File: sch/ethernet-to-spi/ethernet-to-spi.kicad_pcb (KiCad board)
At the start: 2 copper layers, 113 x 32 mm, 34 parts, among them J1 G8X-188S7-BP, J2 mosi, J3 sck_tx, J4 mosi_tx, J5 cs, J6 sck, J7 vcc, J8 gnd, Q1 2N7002, Q2 2N7002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

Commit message: Add level shifters for inputs
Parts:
- added Q3: 2N7002, Package_TO_SOT_SMD:SOT-23, F.Cu at (110.0, 123.6)
- added Q4: 2N7002, Package_TO_SOT_SMD:SOT-23, F.Cu at (109.3, 129.4)
- added R6: 1k, Resistor_SMD:R_0805_2012Metric, F.Cu at (107.3, 119.9)
- added R7: 1k, Resistor_SMD:R_0805_2012Metric, F.Cu at (105.7, 127.8)
- moved C3 7.47 mm to (98.5, 109.9)
- moved C2 6.28 mm to (98.0, 114.1)
- moved C4 4.35 mm to (94.9, 106.7)
- moved U3 4.35 mm to (101.9, 109.9)
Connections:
- U1 pad 1: Net-(J3-Pad1) -> Net-(U1-Pad1)
- U1 pad 2: Net-(J4-Pad1) -> Net-(U1-Pad2)
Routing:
- net VCC: track 179.3 -> 198.9 mm
- net Net-(U1-Pad2): track 0.00 -> 16.6 mm
- net Net-(C3-Pad2): track 14.5 -> 2.50 mm
- net Net-(C2-Pad2): track 14.6 -> 3.59 mm
- net Net-(U1-Pad1): track 0.00 -> 9.73 mm
- net Net-(C3-Pad1): track 10.00 -> 17.7 mm
- net Net-(C2-Pad1): track 7.58 -> 14.3 mm
- net Net-(J4-Pad1): track 9.43 -> 3.38 mm
- net Net-(U1-Pad3): track 36.6 -> 41.0 mm
- net /line: track 50.8 -> 55.2 mm
- net Net-(J1-Pad2): track 21.5 -> 19.2 mm
- net Net-(R2-Pad2): track 13.0 -> 11.3 mm
- net Net-(J3-Pad1): track 4.70 -> 3.06 mm

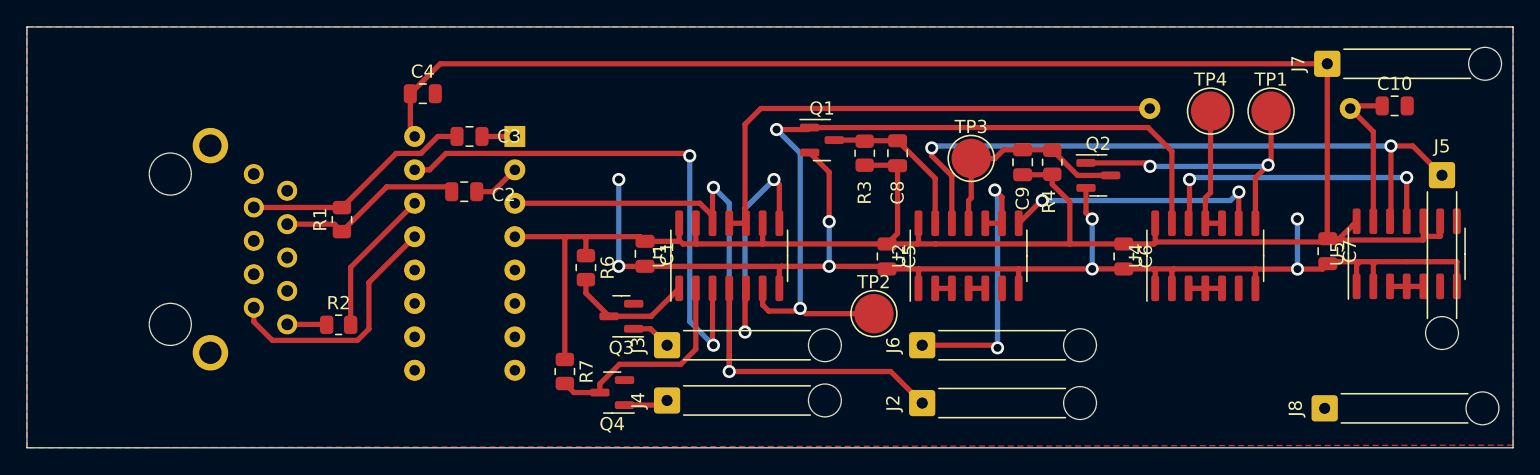
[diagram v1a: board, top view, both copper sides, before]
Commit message: Update capacitor value for 75 nS delay
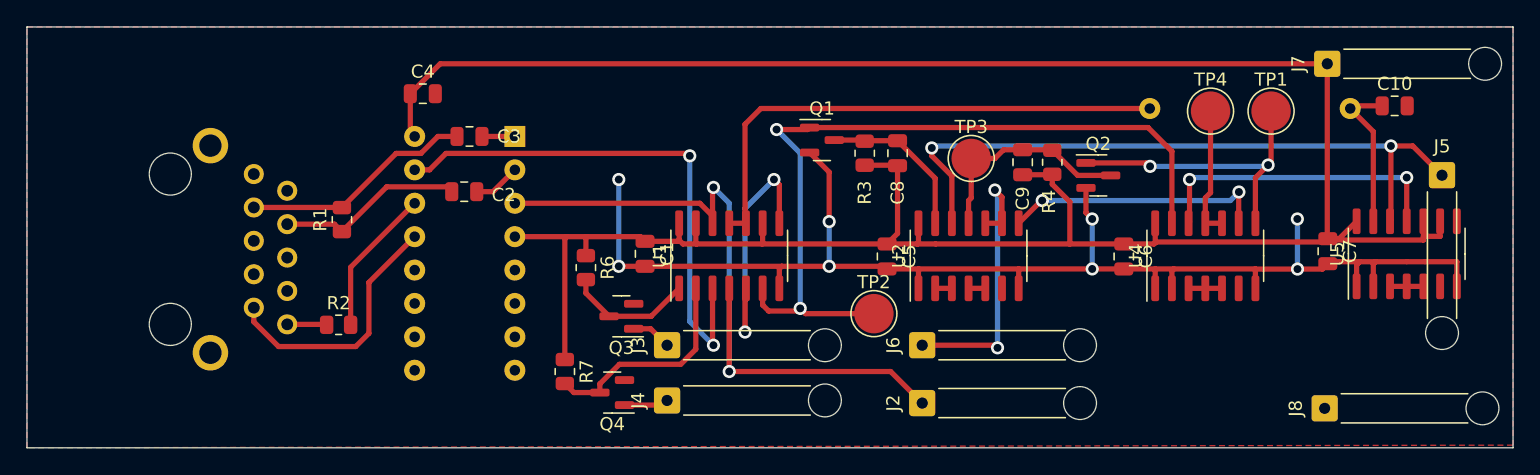
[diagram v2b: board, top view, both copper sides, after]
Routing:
- net Net-(J1-Pad2): track 19.2 -> 19.8 mm
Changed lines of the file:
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@@
     (aux_axis_origin 64.8 133.6)
     (pcbplotparams
-      (layerselection 0x00010fc_ffffffff)
+      (layerselection 0x0001000_7fffffff)
       (disableapertmacros false)
       (usegerberextensions false)
       (usegerberattributes true)
       (usegerberadvancedattributes true)
-      (creategerberjobfile true)
+      (creategerberjobfile false)
       (svguseinch false)
       (svgprecision 6)
@@
       (viasonmask false)
       (mode 1)
-      (useauxorigin false)
+      (useauxorigin true)
       (hpglpennumber 1)
       (hpglpenspeed 20)
@@
       (outputformat 1)
       (mirror false)
-      (drillshape 1)
+      (drillshape 0)
       (scaleselection 1)
-      (outputdirectory "")
+      (outputdirectory "gerber/")
     )
   )
@@
     (fp_line (start 1 -0.625) (end 1 0.625) (layer "F.Fab") (width 0.1))
     (fp_line (start -1 -0.625) (end 1 -0.625) (layer "F.Fab") (width 0.1))
-    (pad "1" smd roundrect (at -0.9125 0 270) (size 1.025 1.4) (layers "F.Cu" "F.Paste" "F.Mask") (roundrect_rratio 0.243902)
+    (pad "1" smd roundrect (at -0.9125 0 270) (size 1.025 1.4) (layers "F.Cu" "F.Paste" "F.Mask") (roundrect_rratio 0.243902439)
       (net 1 "VCC") (pintype "passive"))
-    (pad "2" smd roundrect (at 0.9125 0 270) (size 1.025 1.4) (layers "F.Cu" "F.Paste" "F.Mask") (roundrect_rratio 0.243902)
+    (pad "2" smd roundrect (at 0.9125 0 270) (size 1.025 1.4) (layers "F.Cu" "F.Paste" "F.Mask") (roundrect_rratio 0.243902439)
       (net 42 "Net-(U1-Pad2)") (pintype "passive"))
     (model "${KICAD6_3DMODEL_DIR}/Resistor_SMD.3dshapes/R_0805_2012Metric.wrl"
@@
     (fp_line (start 1 -0.625) (end 1 0.625) (layer "F.Fab") (width 0.1))
     (fp_line (start -1 -0.625) (end 1 -0.625) (layer "F.Fab") (width 0.1))
-    (pad "1" smd roundrect (at -0.9125 0 90) (size 1.025 1.4) (layers "F.Cu" "F.Paste" "F.Mask") (roundrect_rratio 0.243902)
+    (pad "1" smd roundrect (at -0.9125 0 90) (size 1.025 1.4) (layers "F.Cu" "F.Paste" "F.Mask") (roundrect_rratio 0.243902439)
       (net 1 "VCC") (pintype "passive"))
-    (pad "2" smd roundrect (at 0.9125 0 90) (size 1.025 1.4) (layers "F.Cu" "F.Paste" "F.Mask") (roundrect_rratio 0.243902)
+    (pad "2" smd roundrect (at 0.9125 0 90) (size 1.025 1.4) (layers "F.Cu" "F.Paste" "F.Mask") (roundrect_rratio 0.243902439)
       (net 7 "Net-(C8-Pad2)") (pintype "passive"))
     (model "${KICAD6_3DMODEL_DIR}/Resistor_SMD.3dshapes/R_0805_2012Metric.wrl"
@@
     (fp_line (start -1 0.625) (end -1 -0.625) (layer "F.Fab") (width 0.1))
     (fp_line (start 1 0.625) (end -1 0.625) (layer "F.Fab") (width 0.1))
-    (pad "1" smd roundrect (at -0.9125 0 90) (size 1.025 1.4) (layers "F.Cu" "F.Paste" "F.Mask") (roundrect_rratio 0.243902)
+    (pad "1" smd roundrect (at -0.9125 0 90) (size 1.025 1.4) (layers "F.Cu" "F.Paste" "F.Mask") (roundrect_rratio 0.243902439)
       (net 3 "Net-(C2-Pad1)") (pintype "passive"))
-    (pad "2" smd roundrect (at 0.9125 0 90) (size 1.025 1.4) (layers "F.Cu" "F.Paste" "F.Mask") (roundrect_rratio 0.243902)
+    (pad "2" smd roundrect (at 0.9125 0 90) (size 1.025 1.4) (layers "F.Cu" "F.Paste" "F.Mask") (roundrect_rratio 0.243902439)
       (net 5 "Net-(C3-Pad1)") (pintype "passive"))
     (model "${KICAD6_3DMODEL_DIR}/Resistor_SMD.3dshapes/R_0805_2012Metric.wrl"
@@
     (fp_line (start -1 0.625) (end -1 -0.625) (layer "F.Fab") (width 0.1))
     (fp_line (start -1 -0.625) (end 1 -0.625) (layer "F.Fab") (width 0.1))
-    (pad "1" smd roundrect (at -0.9125 0) (size 1.025 1.4) (layers "F.Cu" "F.Paste" "F.Mask") (roundrect_rratio 0.243902)
+    (pad "1" smd roundrect (at -0.9125 0) (size 1.025 1.4) (layers "F.Cu" "F.Paste" "F.Mask") (roundrect_rratio 0.243902439)
       (net 9 "Net-(J1-Pad1)") (pintype "passive"))
-    (pad "2" smd roundrect (at 0.9125 0) (size 1.025 1.4) (layers "F.Cu" "F.Paste" "F.Mask") (roundrect_rratio 0.243902)
+    (pad "2" smd roundrect (at 0.9125 0) (size 1.025 1.4) (layers "F.Cu" "F.Paste" "F.Mask") (roundrect_rratio 0.243902439)
       (net 21 "Net-(R2-Pad2)") (pintype "passive"))
     (model "${KICAD6_3DMODEL_DIR}/Resistor_SMD.3dshapes/R_0805_2012Metric.wrl"
@@
     (fp_line (start 1 -0.625) (end 1 0.625) (layer "F.Fab") (width 0.1))
     (fp_line (start -1 0.625) (end -1 -0.625) (layer "F.Fab") (width 0.1))
-    (pad "1" smd roundrect (at -0.9125 0 90) (size 1.025 1.4) (layers "F.Cu" "F.Paste" "F.Mask") (roundrect_rratio 0.243902)
+    (pad "1" smd roundrect (at -0.9125 0 90) (size 1.025 1.4) (layers "F.Cu" "F.Paste" "F.Mask") (roundrect_rratio 0.243902439)
       (net 1 "VCC") (pintype "passive"))
-    (pad "2" smd roundrect (at 0.9125 0 90) (size 1.025 1.4) (layers "F.Cu" "F.Paste" "F.Mask") (roundrect_rratio 0.243902)
+    (pad "2" smd roundrect (at 0.9125 0 90) (size 1.025 1.4) (layers "F.Cu" "F.Paste" "F.Mask") (roundrect_rratio 0.243902439)
       (net 8 "Net-(C9-Pad2)") (pintype "passive"))
     (model "${KICAD6_3DMODEL_DIR}/Resistor_SMD.3dshapes/R_0805_2012Metric.wrl"
@@
     (fp_line (start 1 0.625) (end -1 0.625) (layer "F.Fab") (width 0.1))
     (fp_line (start -1 -0.625) (end 1 -0.625) (layer "F.Fab") (width 0.1))
-    (pad "1" smd roundrect (at -0.9125 0 270) (size 1.025 1.4) (layers "F.Cu" "F.Paste" "F.Mask") (roundrect_rratio 0.243902)
+    (pad "1" smd roundrect (at -0.9125 0 270) (size 1.025 1.4) (layers "F.Cu" "F.Paste" "F.Mask") (roundrect_rratio 0.243902439)
       (net 1 "VCC") (pintype "passive"))
-    (pad "2" smd roundrect (at 0.9125 0 270) (size 1.025 1.4) (layers "F.Cu" "F.Paste" "F.Mask") (roundrect_rratio 0.243902)
+    (pad "2" smd roundrect (at 0.9125 0 270) (size 1.025 1.4) (layers "F.Cu" "F.Paste" "F.Mask") (roundrect_rratio 0.243902439)
       (net 43 "Net-(U1-Pad1)") (pintype "passive"))
     (model "${KICAD6_3DMODEL_DIR}/Resistor_SMD.3dshapes/R_0805_2012Metric.wrl"
@@
   (segment (start 87.5525 124.215) (end 87.5875 124.25) (width 0.4) (layer "F.Cu") (net 9))
   (segment (start 84.59 124.215) (end 87.5525 124.215) (width 0.4) (layer "F.Cu") (net 9))
+  (segment (start 89.8 125.9) (end 90.8 124.9) (width 0.4) (layer "F.Cu") (net 10))
+  (segment (start 83.92737 125.9) (end 89.8 125.9) (width 0.4) (layer "F.Cu") (net 10))
+  (segment (start 90.8 124.9) (end 90.8 121.025) (width 0.4) (layer "F.Cu") (net 10))
   (segment (start 82.05 122.945) (end 82.05 124.02263) (width 0.4) (layer "F.Cu") (net 10))
-  (segment (start 83.45437 125.427) (end 89.937949 125.427) (width 0.4) (layer "F.Cu") (net 10))
   (segment (start 90.8 121.025) (end 94.28 117.545) (width 0.4) (layer "F.Cu") (net 10))
-  (segment (start 89.937949 125.427) (end 90.8 124.564949) (width 0.4) (layer "F.Cu") (net 10))
-  (segment (start 90.8 124.564949) (end 90.8 121.025) (width 0.4) (layer "F.Cu") (net 10))
-  (segment (start 82.05 124.02263) (end 83.45437 125.427) (width 0.4) (layer "F.Cu") (net 10))
+  (segment (start 82.05 124.02263) (end 83.92737 125.9) (width 0.4) (layer "F.Cu") (net 10))
   (segment (start 130.475 127.8) (end 118.2 127.8) (width 0.4) (layer "F.Cu") (net 16))
   (segment (start 132.875 130.2) (end 130.475 127.8) (width 0.4) (layer "F.Cu") (net 16))
